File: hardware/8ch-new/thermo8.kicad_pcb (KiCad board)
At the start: 4 copper layers, 130 x 137 mm, 267 parts, among them J101 TC CH1-4, J102 TC CH5-8, J401 ENGINE REF FEED/SENSE, J501 AVR ISP, J502 LCD 20x4 HEADER, J503 PANEL BUTTONS, J601 24V IN, J701 TRIP C-NO-NC, J702 ALM C-NO-NC, J703 RS485 A B GND, K701 G6K-2F-Y DC5, K702 G6K-2F-Y DC5, Q401 2N7002, Q402 MMBT3906, Q701 2N7002, Q702 2N7002, SW501 UP, SW502 DOWN, SW503 SET, SW504 ESC, SW505 ACK, U101 AD7124-8BCPZ, U102 TMP126DCKR, U103 TMP126DCKR, U401 B0505S-1WR2, U402 LP2985IM5X-3.3, U403 CA-IS3761HW, U404 CA-IS3761HW, U406 REF3030AIDBZR, U407 MCP6001T-I/OT, U408 TLV7031DBVR, U409 TL431, U411 74LVC1G125, U501 ATmega1284P-AU, U601 LM5164DDAR, U703 ADM2587EBRWZ, Y501 8MHz

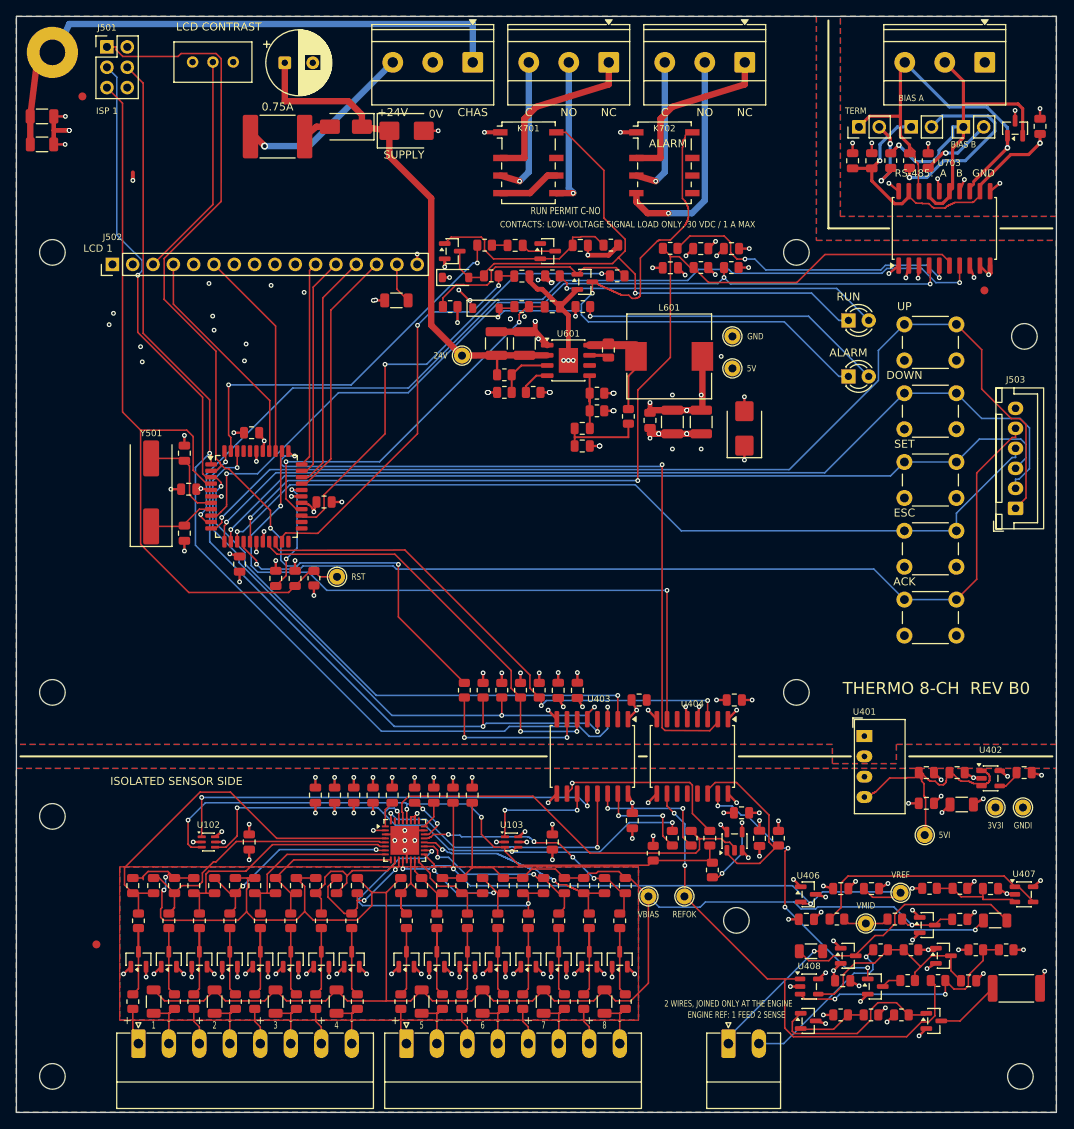
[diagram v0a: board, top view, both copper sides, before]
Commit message: 8ch REV B0: overlapping drill holes and vias in SMD lands fixed (I-131)
12 hole_to_hole + 11 co-located holes and 3 vias into lands removed/moved; DRC 0/0/0
with hole rules as errors, pincaps 0. Release 8ch-revb0-20261019-042934-2d12ea.

Co-Authored-By: Claude Opus 5.5 <noreply@anthropic.com>
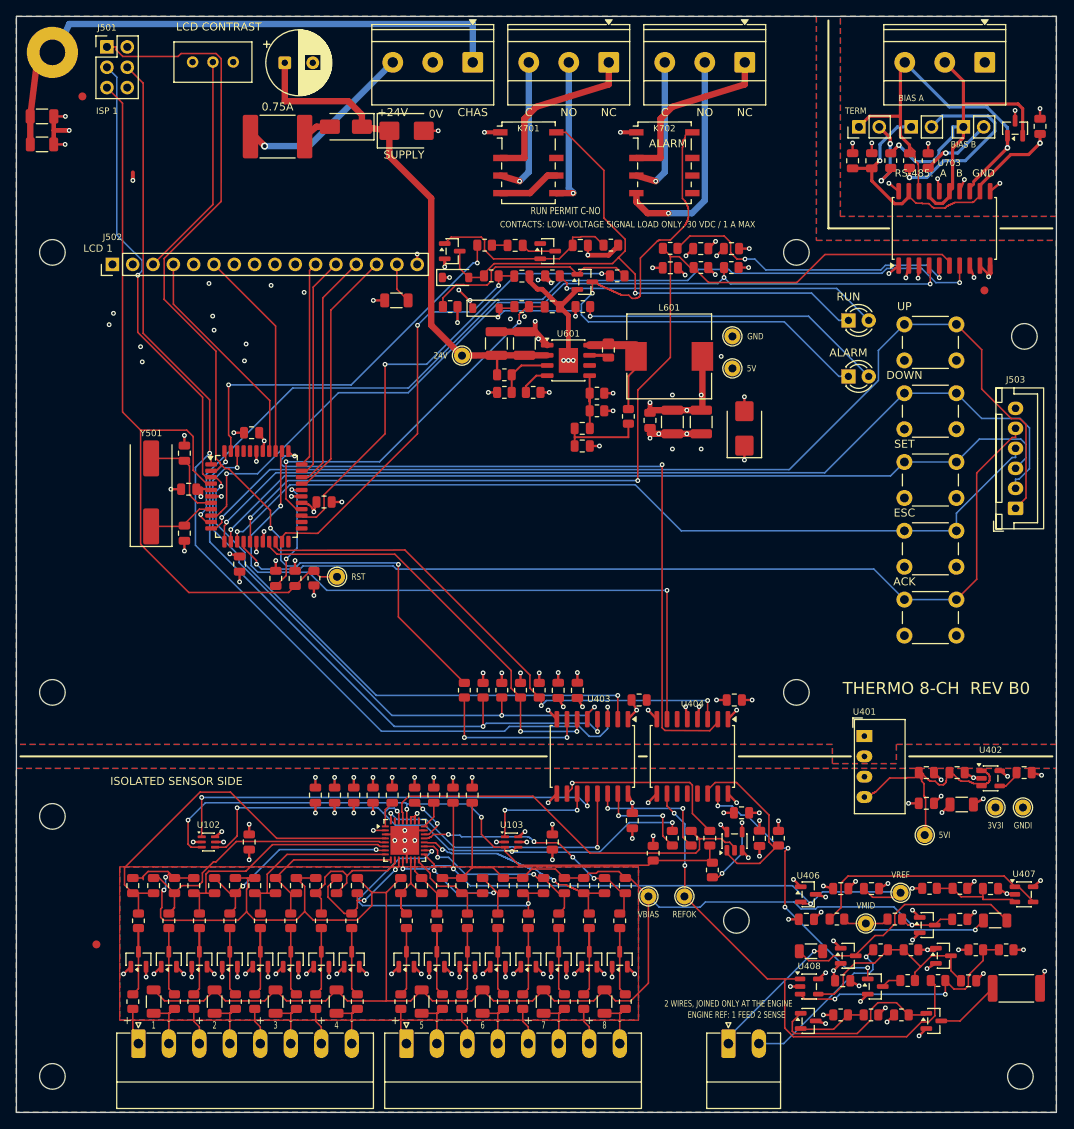
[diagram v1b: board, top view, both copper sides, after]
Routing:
- net +5V: track 61.4 -> 62.4 mm, vias 49 -> 42
- net GND: track 99.5 -> 99.8 mm, vias 69 -> 58
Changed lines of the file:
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@@
 	)
 	(segment
-		(start 44.9 35.45)
-		(end 44.9 35.45)
-		(width 0.25)
-		(layer "F.Cu")
-		(net "+5V")
-	)
-	(segment
 		(start 37 61.5)
 		(end 37 61.55)
@@
 	)
 	(segment
-		(start 66.95 33.25)
-		(end 66.95 33.25)
-		(width 0.25)
-		(layer "F.Cu")
-		(net "+5V")
-	)
-	(segment
 		(start 66.0925 32.5425)
 		(end 66.0925 32.435)
@@
 	)
 	(segment
+		(start 23.0627 59.0199)
+		(end 23.06 60.025)
+		(width 0.6)
+		(layer "F.Cu")
+		(net "+5V")
+	)
+	(segment
 		(start 88.435 29.025)
 		(end 87.5334 29.9266)
@@
 	)
 	(via
-		(at 23.0627 59.0199)
+		(at 23.06 60.025)
 		(size 0.6)
 		(drill 0.3)
@@
 	)
 	(via
-		(at 72.88 53.7)
-		(size 0.6)
-		(drill 0.3)
-		(layers "F.Cu" "B.Cu")
-		(net "+5V")
-	)
-	(via
 		(at 60.675 82.0625)
 		(size 0.6)
@@
 	)
 	(via
-		(at 72.955 53.7)
-		(size 0.6)
-		(drill 0.3)
-		(layers "F.Cu" "B.Cu")
-		(net "+5V")
-	)
-	(via
-		(at 44.9 35.45)
-		(size 0.6)
-		(drill 0.3)
-		(layers "F.Cu" "B.Cu")
-		(net "+5V")
-	)
-	(via
 		(at 54.144999 32.634999)
 		(size 0.6)
@@
 	)
 	(via
-		(at 74.7325 47.1)
-		(size 0.6)
-		(drill 0.3)
-		(layers "F.Cu" "B.Cu")
-		(net "+5V")
-	)
-	(via
 		(at 11.595 38.535)
 		(size 0.6)
@@
 	)
 	(via
-		(at 74.583 47.1)
-		(size 0.6)
-		(drill 0.3)
-		(layers "F.Cu" "B.Cu")
-		(net "+5V")
-	)
-	(via
 		(at 44.6125 35.5)
 		(size 0.6)
@@
 	)
 	(via
-		(at 83.8 49.225)
-		(size 0.6)
-		(drill 0.3)
-		(layers "F.Cu" "B.Cu")
-		(net "+5V")
-	)
-	(via
 		(at 66.85 33.3)
 		(size 0.6)
@@
 	)
 	(via
-		(at 66.95 33.25)
-		(size 0.6)
-		(drill 0.3)
-		(layers "F.Cu" "B.Cu")
-		(net "+5V")
-	)
-	(via
 		(at 87.515 85.45)
 		(size 0.6)
@@
 	)
 	(segment
+		(start 121.533 32.2885)
+		(end 121.533 32.549999)
+		(width 0.6)
+		(layer "F.Cu")
+		(net "GND")
+	)
+	(segment
 		(start 50.925 14.295)
 		(end 52.725 14.295)
@@
 	)
 	(via
-		(at 74.7325 49.3)
-		(size 0.6)
-		(drill 0.3)
-		(layers "F.Cu" "B.Cu")
-		(net "GND")
-	)
-	(via
 		(at 24.0731 33.3786)
 		(size 0.6)
@@
 	)
 	(via
-		(at 58.8375 47)
-		(size 0.6)
-		(drill 0.3)
-		(layers "F.Cu" "B.Cu")
-		(net "GND")
-	)
-	(via
 		(at 109.063 32.144)
 		(size 0.6)
@@
 	)
 	(via
-		(at 74.583 49.3)
+		(at 52.725 14.295)
 		(size 0.6)
 		(drill 0.3)
@@
 	)
 	(via
-		(at 52.725 14.295)
+		(at 121.533 32.549999)
 		(size 0.6)
 		(drill 0.3)
@@
 	)
 	(via
-		(at 64.849999 38.115)
-		(size 0.6)
-		(drill 0.3)
-		(layers "F.Cu" "B.Cu")
-		(net "GND")
-	)
-	(via
 		(at 12.1331 37.1114)
 		(size 0.6)
@@
 	)
 	(via
-		(at 121.533 32.2885)
-		(size 0.6)
-		(drill 0.3)
-		(layers "F.Cu" "B.Cu")
-		(net "GND")
-	)
-	(via
-		(at 66.613 47)
-		(size 0.6)
-		(drill 0.3)
-		(layers "F.Cu" "B.Cu")
-		(net "GND")
-	)
-	(via
 		(at 83.6519 86.2895)
 		(size 0.6)
@@
 	)
 	(via
-		(at 61.75 37.815)
-		(size 0.6)
-		(drill 0.3)
-		(layers "F.Cu" "B.Cu")
-		(net "GND")
-	)
-	(via
 		(at 14.56 20.5)
 		(size 0.6)
@@
 	)
 	(via
-		(at 6.6 14.25)
-		(size 0.6)
-		(drill 0.3)
-		(layers "F.Cu" "B.Cu")
-		(net "GND")
-	)
-	(via
 		(at 63.5 37.515)
 		(size 0.6)
@@
 	)
 	(via
-		(at 66.7625 47)
-		(size 0.6)
-		(drill 0.3)
-		(layers "F.Cu" "B.Cu")
-		(net "GND")
-	)
-	(via
-		(at 58.987 47)
-		(size 0.6)
-		(drill 0.3)
-		(layers "F.Cu" "B.Cu")
-		(net "GND")
-	)
-	(via
 		(at 112.706 32.7205)
 		(size 0.6)
@@
 	)
 	(via
-		(at 83.8 52.175)
-		(size 0.6)
-		(drill 0.3)
-		(layers "F.Cu" "B.Cu")
-		(net "GND")
-	)
-	(via
-		(at 80.3 52.175)
-		(size 0.6)
-		(drill 0.3)
-		(layers "F.Cu" "B.Cu")
-		(net "GND")
-	)
-	(via
 		(at 85.3481 86.2895)
 		(size 0.6)
@@
 	)
 	(segment
+		(start 113.987 116.675)
+		(end 113.887 116.675)
+		(width 0.5)
+		(layer "F.Cu")
+		(net "GND_ISO")
+	)
+	(segment
 		(start 97.9575 121.265)
 		(end 96.745 121.265)
@@
 	)
 	(via
-		(at 113.987 116.675)
+		(at 91.4922 105.163)
 		(size 0.6)
 		(drill 0.3)
@@
 	)
 	(via
-		(at 91.4922 105.163)
+		(at 49.775 95.12)
 		(size 0.6)
 		(drill 0.3)
@@
 	)
 	(via
-		(at 49.775 95.12)
+		(at 42.175 95.12)
 		(size 0.6)
 		(drill 0.3)
@@
 	)
 	(via
-		(at 42.175 95.12)
+		(at 102.133 115.559)
 		(size 0.6)
 		(drill 0.3)
@@
 	)
 	(via
-		(at 102.133 115.559)
+		(at 113.887 116.675)
 		(size 0.6)
 		(drill 0.3)

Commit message: 40ch, 8ch-new: dangling trims, 8ch-new I-129 relay rule; re-released 141240 / 141437 under the new warning gate; I-129, I-131 closed
40ch: DRC 0/0/0, warnings 3 silk, pincaps 0, holes 0, fill 1212/1212, MANIFEST 76/76.
8ch-new: DRC 0/0/0, warnings silk only, pincaps 0, holes 0, fill 496/496, MANIFEST 56/56.

Co-Authored-By: Claude Opus 5.5 <noreply@anthropic.com>
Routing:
- net /ISOLATION_1/DOUT_ISO_RAW: track 23.4 -> 23.5 mm, vias 1 -> 0
- net /OUTPUTS/+3V3_RS485: vias 2 -> 1
- net +5V: vias 42 -> 36
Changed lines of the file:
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@@
 	)
 	(via
-		(at 28.5086 43.0589)
-		(size 0.6)
-		(drill 0.3)
-		(layers "F.Cu" "B.Cu")
-		(net "+5V")
-	)
-	(via
 		(at 26.6684 67.18)
 		(size 0.6)
@@
 	)
 	(via
-		(at 15.7318 43.1882)
-		(size 0.6)
-		(drill 0.3)
-		(layers "F.Cu" "B.Cu")
-		(net "+5V")
-	)
-	(via
 		(at 65.355 82.0625)
 		(size 0.6)
@@
 	)
 	(via
-		(at 24.7086 39.2189)
-		(size 0.6)
-		(drill 0.3)
-		(layers "F.Cu" "B.Cu")
-		(net "+5V")
-	)
-	(via
-		(at 11.595 38.535)
-		(size 0.6)
-		(drill 0.3)
-		(layers "F.Cu" "B.Cu")
-		(net "+5V")
-	)
-	(via
 		(at 58.5 14.49)
 		(size 0.6)
@@
 	)
 	(via
-		(at 82 47.325)
-		(size 0.6)
-		(drill 0.3)
-		(layers "F.Cu" "B.Cu")
-		(net "+5V")
-	)
-	(via
 		(at 69.8925 37.475)
 		(size 0.6)
@@
 	)
 	(via
-		(at 88.1 42.5)
-		(size 0.6)
-		(drill 0.3)
-		(layers "F.Cu" "B.Cu")
-		(net "+5V")
-	)
-	(via
 		(at 65.2 32.95)
 		(size 0.6)
@@
 	)
 	(segment
-		(start 15.8547 107.7)
-		(end 15.8547 107.9143)
-		(width 0.2)
-		(layer "F.Cu")
-		(net "V_BIAS")
-	)
-	(segment
 		(start 79 110)
 		(end 76.7 107.7)
@@
 	)
 	(via
-		(at 127.955 15.8402)
-		(size 0.7)
-		(drill 0.35)
-		(layers "F.Cu" "B.Cu")
-		(net "/OUTPUTS/+3V3_RS485")
-	)
-	(via
 		(at 107.954 18.046)
 		(size 0.6)
@@
 	)
 	(segment
-		(start 68.825 97.15)
-		(end 69.4751 96.4999)
+		(start 69.4751 95.8335)
+		(end 69.549 95.7596)
 		(width 0.2)
 		(layer "F.Cu")
 		(net "/ISOLATION_1/DOUT_ISO_RAW")
 	)
-	(via
-		(at 69.4751 95.8335)
-		(size 0.6)
-		(drill 0.3)
-		(layers "F.Cu" "B.Cu")
+	(segment
+		(start 68.825 97.15)
+		(end 69.4751 96.4999)
+		(width 0.2)
+		(layer "F.Cu")
 		(net "/ISOLATION_1/DOUT_ISO_RAW")
 	)
